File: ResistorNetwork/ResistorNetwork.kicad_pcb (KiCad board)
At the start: 2 copper layers, 110 x 50 mm, 22 parts, among them J1 Conn_01x02_Female, J2 Conn_01x02_Female, J3 Conn_01x02_Female, K1 DBR72410

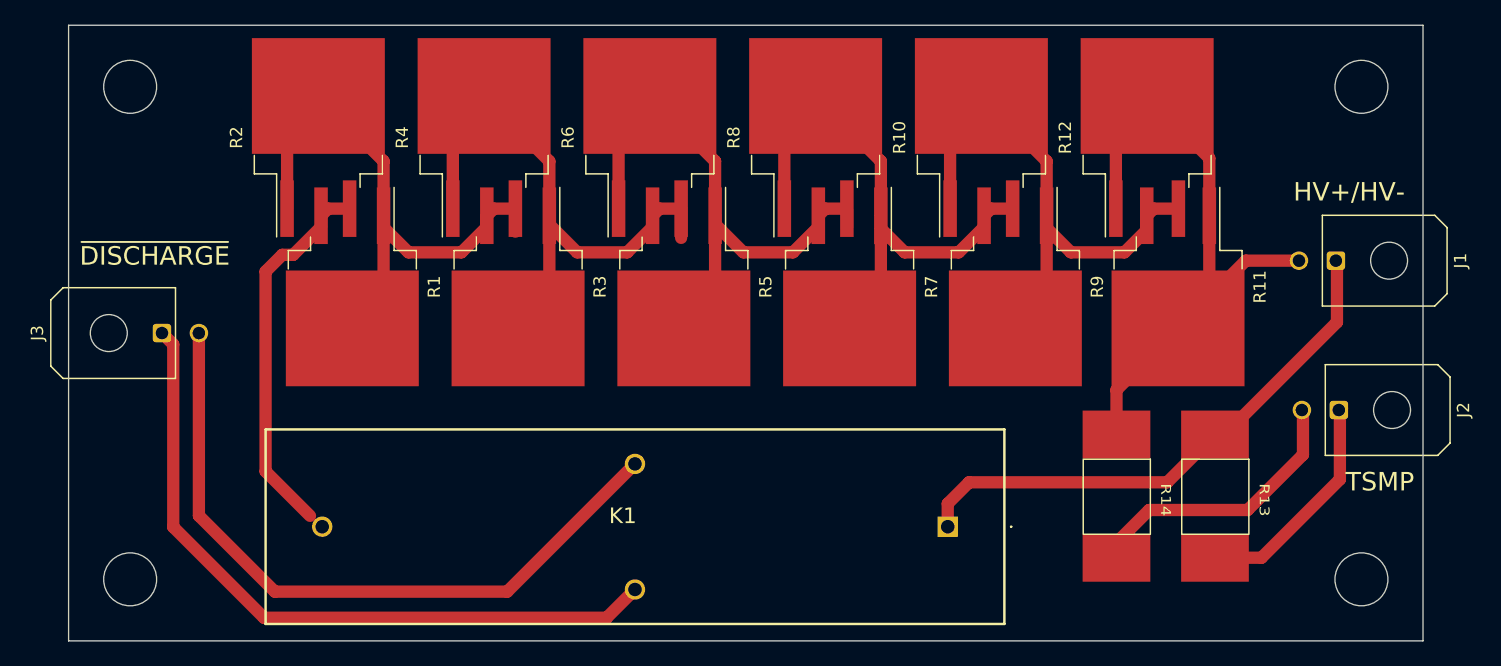
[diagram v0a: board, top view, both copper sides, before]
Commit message: updates to silkscreen for resistor network
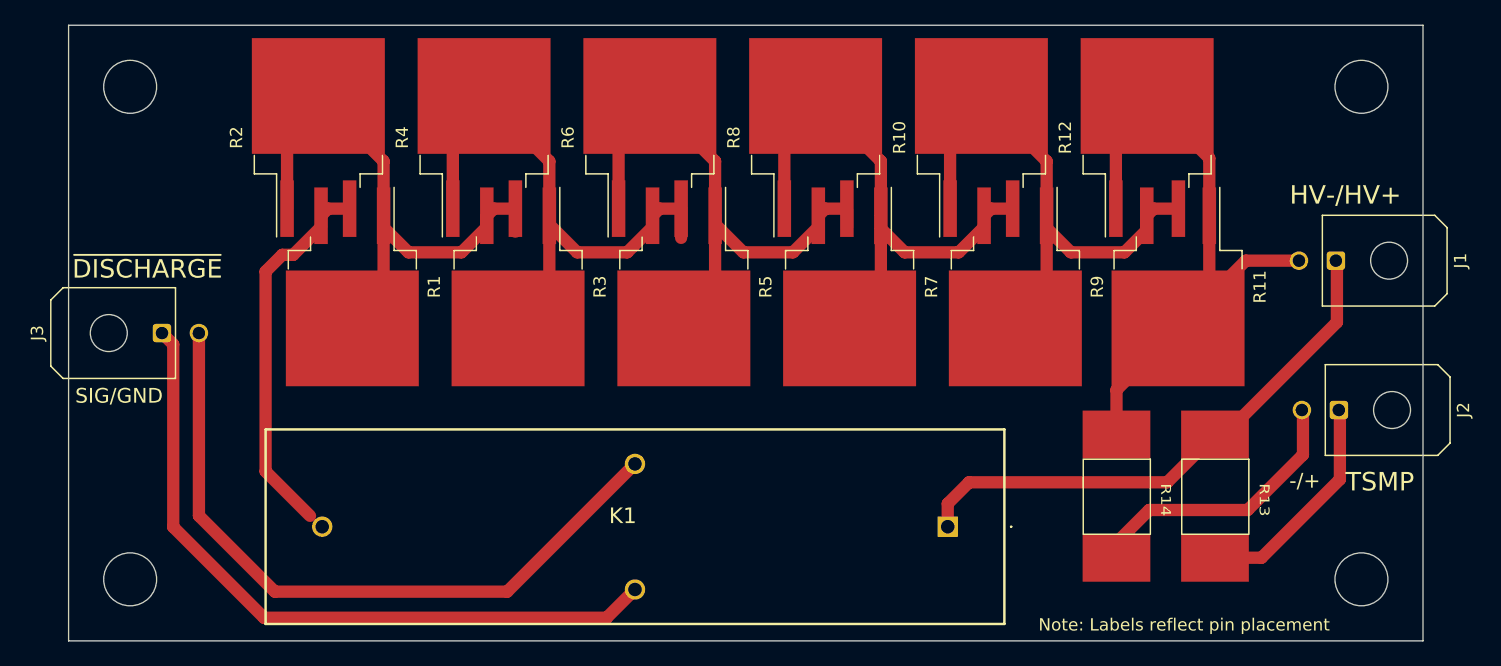
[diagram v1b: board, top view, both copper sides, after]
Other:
- board text added: "-/+"
- board text added: "HV-/HV+"
- board text added: "Note: Labels reflect pin placement"
- board text added: "SIG/GND"
- board text removed: "HV+/HV-"
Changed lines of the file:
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@@
   )
   (gr_rect (start 26 28) (end 136 78) (layer "Edge.Cuts") (width 0.1) (fill none))
+  (gr_text "-/+\n" (at 126.4 65) (layer "F.SilkS")
+    (effects (font (size 1.2 1.2) (thickness 0.15)))
+  )
+  (gr_text "SIG/GND\n" (at 30.1 58.1) (layer "F.SilkS")
+    (effects (font (size 1.2 1.2) (thickness 0.15)))
+  )
   (gr_text "TSMP\n\n\n" (at 132.5 67.5) (layer "F.SilkS")
     (effects (font (size 1.5 1.5) (thickness 0.15)))
   )
-  (gr_text "HV+/HV-\n\n" (at 130 42.75) (layer "F.SilkS")
+  (gr_text "HV-/HV+\n\n" (at 129.7 43) (layer "F.SilkS")
     (effects (font (size 1.5 1.5) (thickness 0.15)))
   )
-  (gr_text "~{DISCHARGE}\n" (at 33 46.75) (layer "F.SilkS")
+  (gr_text "Note: Labels reflect pin placement\n\n" (at 116.6 77.5) (layer "F.SilkS")
+    (effects (font (size 1 1) (thickness 0.15)))
+  )
+  (gr_text "~{DISCHARGE}\n" (at 32.4 47.8) (layer "F.SilkS")
     (effects (font (size 1.5 1.5) (thickness 0.15)))
   )

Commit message: added contactor fuse
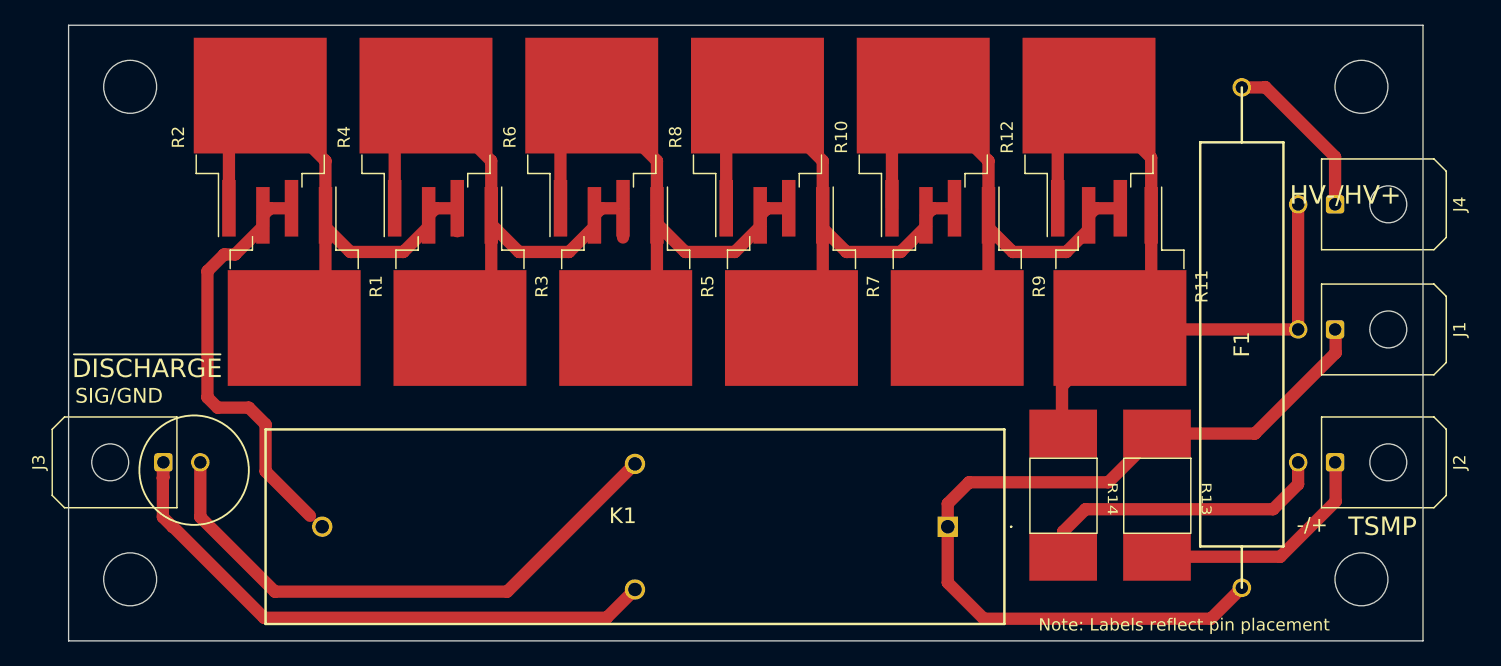
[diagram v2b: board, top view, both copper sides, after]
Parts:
- added F1: 0ADAP1000-RE, SamacSys_Parts:0ADAP1000RE, F.Cu at (121.3, 75.4)
- added J4: Conn_01x02_Female, Connector_Molex:Molex_Micro-Fit_3.0_43045-0200_2x01_P3.00mm_Horizontal, F.Cu at (128.9, 42.5)
- moved J3 10.5 mm to (33.7, 63.5)
- moved J1 5.59 mm to (128.9, 52.7)
- moved R11 4.72 mm to (111.4, 49.2)
- moved R12 4.72 mm to (108.9, 37.1)
- moved R3 4.72 mm to (57.8, 49.2)
- moved R5 4.72 mm to (71.2, 49.2)
- moved R6 4.72 mm to (68.5, 37.1)
- moved R7 4.72 mm to (84.7, 49.2)
- moved R8 4.72 mm to (82.0, 37.1)
- moved R1 4.72 mm to (44.3, 49.2)
- moved R2 4.72 mm to (41.6, 37.1)
- moved R4 4.72 mm to (55.0, 37.1)
- moved R10 4.72 mm to (95.4, 37.1)
- moved R9 4.72 mm to (98.2, 49.2)
- moved R13 4.71 mm to (111.6, 59.2)
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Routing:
- net /HV+: track 44.6 -> 71.1 mm
- net Net-(F1-Pad2): track 0.00 -> 13.8 mm
- net /HV-: track 55.0 -> 67.5 mm
- net GND: track 57.1 -> 46.6 mm
- net /~{Discharge}: track 57.6 -> 47.8 mm
- net Net-(K1-Pad2): track 32.2 -> 35.6 mm
- net /HV-_TSMP: track 22.9 -> 24.5 mm
- net /HV+_TSMP: track 18.8 -> 19.6 mm

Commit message: fixed routing error oops
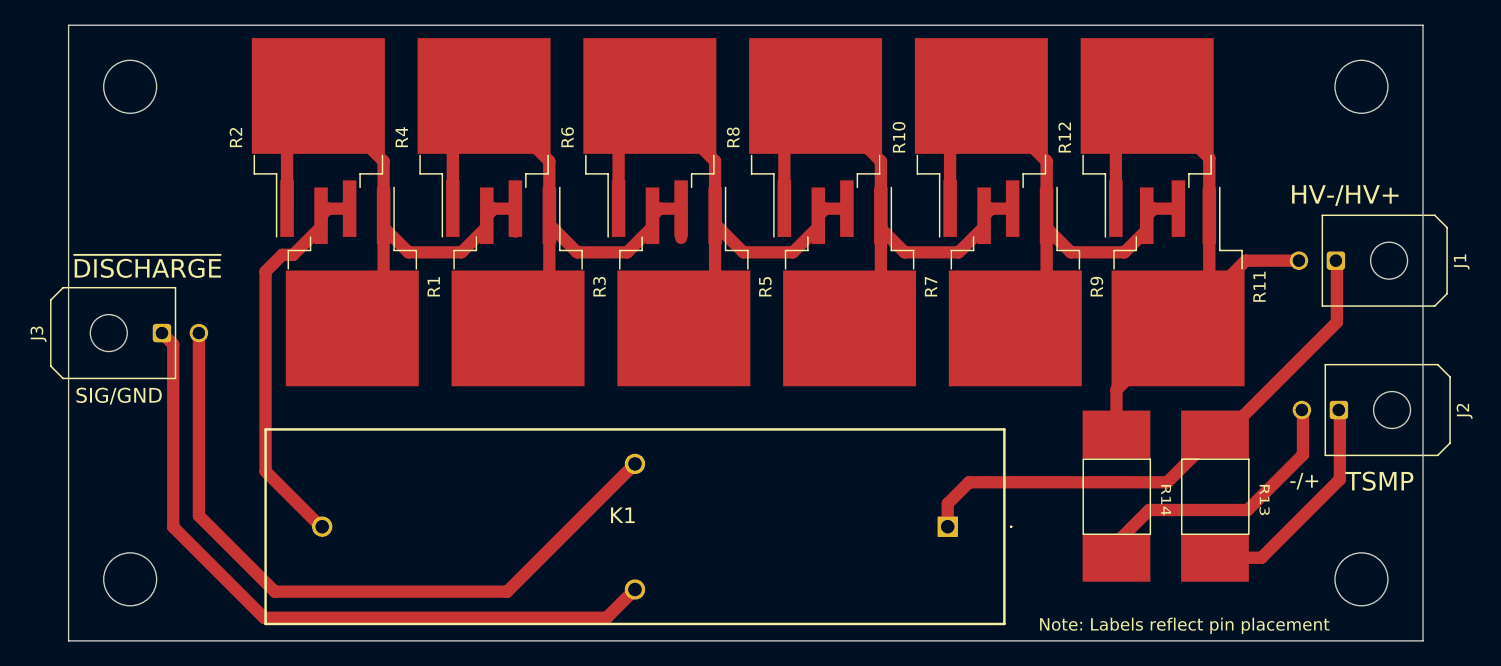
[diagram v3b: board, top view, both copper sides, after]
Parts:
- removed F1: 0ADAP1000-RE, SamacSys_Parts:0ADAP1000RE
- removed J4: Conn_01x02_Female, Connector_Molex:Molex_Micro-Fit_3.0_43045-0200_2x01_P3.00mm_Horizontal
- moved J3 10.5 mm to (33.6, 53.0)
- moved J1 5.59 mm to (128.9, 47.1)
- moved R11 4.72 mm to (116.1, 49.2)
- moved R12 4.72 mm to (113.6, 37.1)
- moved R3 4.72 mm to (62.5, 49.2)
- moved R5 4.72 mm to (76.0, 49.2)
- moved R6 4.72 mm to (73.2, 37.1)
- moved R7 4.72 mm to (89.4, 49.2)
- moved R8 4.72 mm to (86.7, 37.1)
- moved R1 4.72 mm to (49.0, 49.2)
- moved R2 4.72 mm to (46.3, 37.1)
- moved R4 4.72 mm to (59.7, 37.1)
- moved R10 4.72 mm to (100.1, 37.1)
- moved R9 4.72 mm to (102.9, 49.2)
- moved R13 4.71 mm to (116.4, 59.3)
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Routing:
- net /HV+: track 71.1 -> 44.6 mm
- net Net-(F1-Pad2): track 13.8 -> 0.00 mm
- net /HV-: track 67.5 -> 55.0 mm
- net GND: track 46.6 -> 57.1 mm
- net /~{Discharge}: track 47.8 -> 57.6 mm
- net Net-(R1-Pad2): track 35.6 -> 33.5 mm
- net /HV-_TSMP: track 24.5 -> 22.9 mm
- net /HV+_TSMP: track 19.6 -> 18.8 mm
